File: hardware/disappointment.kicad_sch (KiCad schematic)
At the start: 60 parts, among them J1 Bus_ISA_16bit, J3 Conn_02x10_Odd_Even, J5 ATX-24, U1 F85226AF, U2 L7905

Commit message: pson
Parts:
- added J2: Conn_01x02_Pin, Connector_PinHeader_2.54mm:PinHeader_1x02_P2.54mm_Vertical, symbol Connector:Conn_01x02_Pin
- added R16: 4.7K, Resistor_SMD:R_1206_3216Metric_Pad1.30x1.75mm_HandSolder, symbol Device:R_Small
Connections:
- net +3.3V: now also R16.1
- net GND: now also J2.2 (Pin_2)
- net PWRDN#: now also R16.2
- net at J5.16 (PS_ON#): now also J2.1 (Pin_1)
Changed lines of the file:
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@@
     (stroke (width 0) (type default))
   )
+  (wire (pts (xy 306.07 144.78) (xy 309.88 144.78))
+    (stroke (width 0) (type default))
+  )
   (wire (pts (xy 478.79 162.56) (xy 481.33 162.56))
     (stroke (width 0) (type default))
@@
     (stroke (width 0) (type default))
   )
-  (wire (pts (xy 313.69 264.16) (xy 321.31 264.16))
+  (wire (pts (xy 309.88 264.16) (xy 321.31 264.16))
     (stroke (width 0) (type default))
   )
@@
     )
   )
+  (symbol (lib_name "+3.3V_9") (lib_id "power:+3.3V") (at 309.88 259.08 0) (unit 1)
+    (in_bom yes) (on_board yes) (dnp no) (fields_autoplaced)
+    (property "Reference" "#PWR018" (at 309.88 262.89 0)
+      (effects (font (size 1.27 1.27)) hide)
+    )
+    (property "Value" "+3.3V" (at 309.88 255.27 0)
+      (effects (font (size 1.27 1.27)))
+    )
+    (property "Footprint" "" (at 309.88 259.08 0)
+      (effects (font (size 1.27 1.27)) hide)
+    )
+    (property "Datasheet" "" (at 309.88 259.08 0)
+      (effects (font (size 1.27 1.27)) hide)
+    )
+    (pin "1")
+    (instances
+      (project "disappointment"
+        (path "/a1292a79-9ba8-4ff9-9f33-166186bea326"
+          (reference "#PWR018") (unit 1)
+        )
+      )
+    )
+  )
   (symbol (lib_name "GND_4") (lib_id "power:GND") (at 331.47 209.55 0) (unit 1)
     (in_bom yes) (on_board yes) (dnp no)
@@
     )
   )
+  (symbol (lib_name "GND_3") (lib_id "power:GND") (at 306.07 147.32 0) (unit 1)
+    (in_bom yes) (on_board yes) (dnp no) (fields_autoplaced)
+    (property "Reference" "#PWR019" (at 306.07 153.67 0)
+      (effects (font (size 1.27 1.27)) hide)
+    )
+    (property "Value" "GND" (at 306.07 152.4 0)
+      (effects (font (size 1.27 1.27)) hide)
+    )
+    (property "Footprint" "" (at 306.07 147.32 0)
+      (effects (font (size 1.27 1.27)) hide)
+    )
+    (property "Datasheet" "" (at 306.07 147.32 0)
+      (effects (font (size 1.27 1.27)) hide)
+    )
+    (pin "1")
+    (instances
+      (project "disappointment"
+        (path "/a1292a79-9ba8-4ff9-9f33-166186bea326"
+          (reference "#PWR019") (unit 1)
+        )
+      )
+    )
+  )
   (symbol (lib_id "Device:R_Pack04") (at 476.25 170.18 90) (unit 1)
     (in_bom yes) (on_board yes) (dnp no)
@@
     )
   )
+  (symbol (lib_id "Connector:Conn_01x02_Pin") (at 300.99 144.78 0) (unit 1)
+    (in_bom yes) (on_board yes) (dnp no)
+    (property "Reference" "J2" (at 300.99 135.89 0)
+      (effects (font (size 1.27 1.27)))
+    )
+    (property "Value" "Conn_01x02_Pin" (at 299.72 138.43 0)
+      (effects (font (size 1.27 1.27)))
+    )
+    (property "Footprint" "Connector_PinHeader_2.54mm:PinHeader_1x02_P2.54mm_Vertical" (at 300.99 144.78 0)
+      (effects (font (size 1.27 1.27)) hide)
+    )
+    (property "Datasheet" "~" (at 300.99 144.78 0)
+      (effects (font (size 1.27 1.27)) hide)
+    )
+    (pin "1")
+    (pin "2")
+    (instances
+      (project "disappointment"
+        (path "/a1292a79-9ba8-4ff9-9f33-166186bea326"
+          (reference "J2") (unit 1)
+        )
+      )
+    )
+  )
   (symbol (lib_id "Device:R_Small") (at 407.67 152.4 270) (unit 1)
     (in_bom yes) (on_board yes) (dnp no)
@@
         )
       )
+    )
+  )
+  (symbol (lib_id "Device:R_Small") (at 309.88 261.62 0) (unit 1)
+    (in_bom yes) (on_board yes) (dnp no)
+    (property "Reference" "R16" (at 307.34 266.7 90)
+      (effects (font (size 1.27 1.27)) (justify left))
+    )
+    (property "Value" "4.7K" (at 307.34 261.62 90)
+      (effects (font (size 1.27 1.27)) (justify left))
+    )
+    (property "Footprint" "Resistor_SMD:R_1206_3216Metric_Pad1.30x1.75mm_HandSolder" (at 309.88 261.62 0)
+      (effects (font (size 1.27 1.27)) hide)
+    )
+    (property "Datasheet" "~" (at 309.88 261.62 0)
+      (effects (font (size 1.27 1.27)) hide)
+    )
+    (pin "1")
+    (pin "2")
+    (instances
+      (project "disappointment"
+        (path "/a1292a79-9ba8-4ff9-9f33-166186bea326"
+          (reference "R16") (unit 1)
+        )
+      )

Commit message: what a... letdown?
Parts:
- J2: value Conn_01x02_Pin -> PS_ON
- J3: value Conn_02x10_Odd_Even -> LPC
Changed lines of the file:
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@@
   (junction (at 396.24 167.64) (diameter 0) (color 0 0 0 0)
   )
-  (junction (at 345.44 149.86) (diameter 0) (color 0 0 0 0)
-  )
   (junction (at 481.33 193.04) (diameter 0) (color 0 0 0 0)
   )
   (junction (at 124.46 224.79) (diameter 0) (color 0 0 0 0)
   )
-  (junction (at 345.44 152.4) (diameter 0) (color 0 0 0 0)
-  )
   (junction (at 124.46 186.69) (diameter 0) (color 0 0 0 0)
   )
@@
     (stroke (width 0) (type default))
   )
-  (wire (pts (xy 340.36 152.4) (xy 345.44 152.4))
-    (stroke (width 0) (type default))
-  )
   (wire (pts (xy 416.56 139.7) (xy 425.45 139.7))
     (stroke (width 0) (type default))
@@
     (stroke (width 0) (type default))
   )
-  (wire (pts (xy 339.09 149.86) (xy 345.44 149.86))
-    (stroke (width 0) (type default))
-  )
   (label "IRQ7" (at 425.45 190.5 180) (fields_autoplaced)
     (effects (font (size 1.27 1.27)) (justify right bottom))
@@
       (effects (font (size 1.27 1.27)))
     )
-    (property "Value" "Conn_01x02_Pin" (at 299.72 138.43 0)
+    (property "Value" "PS_ON" (at 299.72 138.43 0)
       (effects (font (size 1.27 1.27)))
     )
@@
   (symbol (lib_id "Connector_Generic:Conn_02x10_Odd_Even") (at 326.39 251.46 0) (unit 1)
     (in_bom yes) (on_board yes) (dnp no) (fields_autoplaced)
-    (property "Reference" "J3" (at 327.66 234.95 0)
+    (property "Reference" "J3" (at 327.66 236.22 0)
       (effects (font (size 1.27 1.27)))
     )
-    (property "Value" "Conn_02x10_Odd_Even" (at 327.66 237.49 0)
+    (property "Value" "LPC" (at 327.66 238.76 0)
       (effects (font (size 1.27 1.27)))
     )

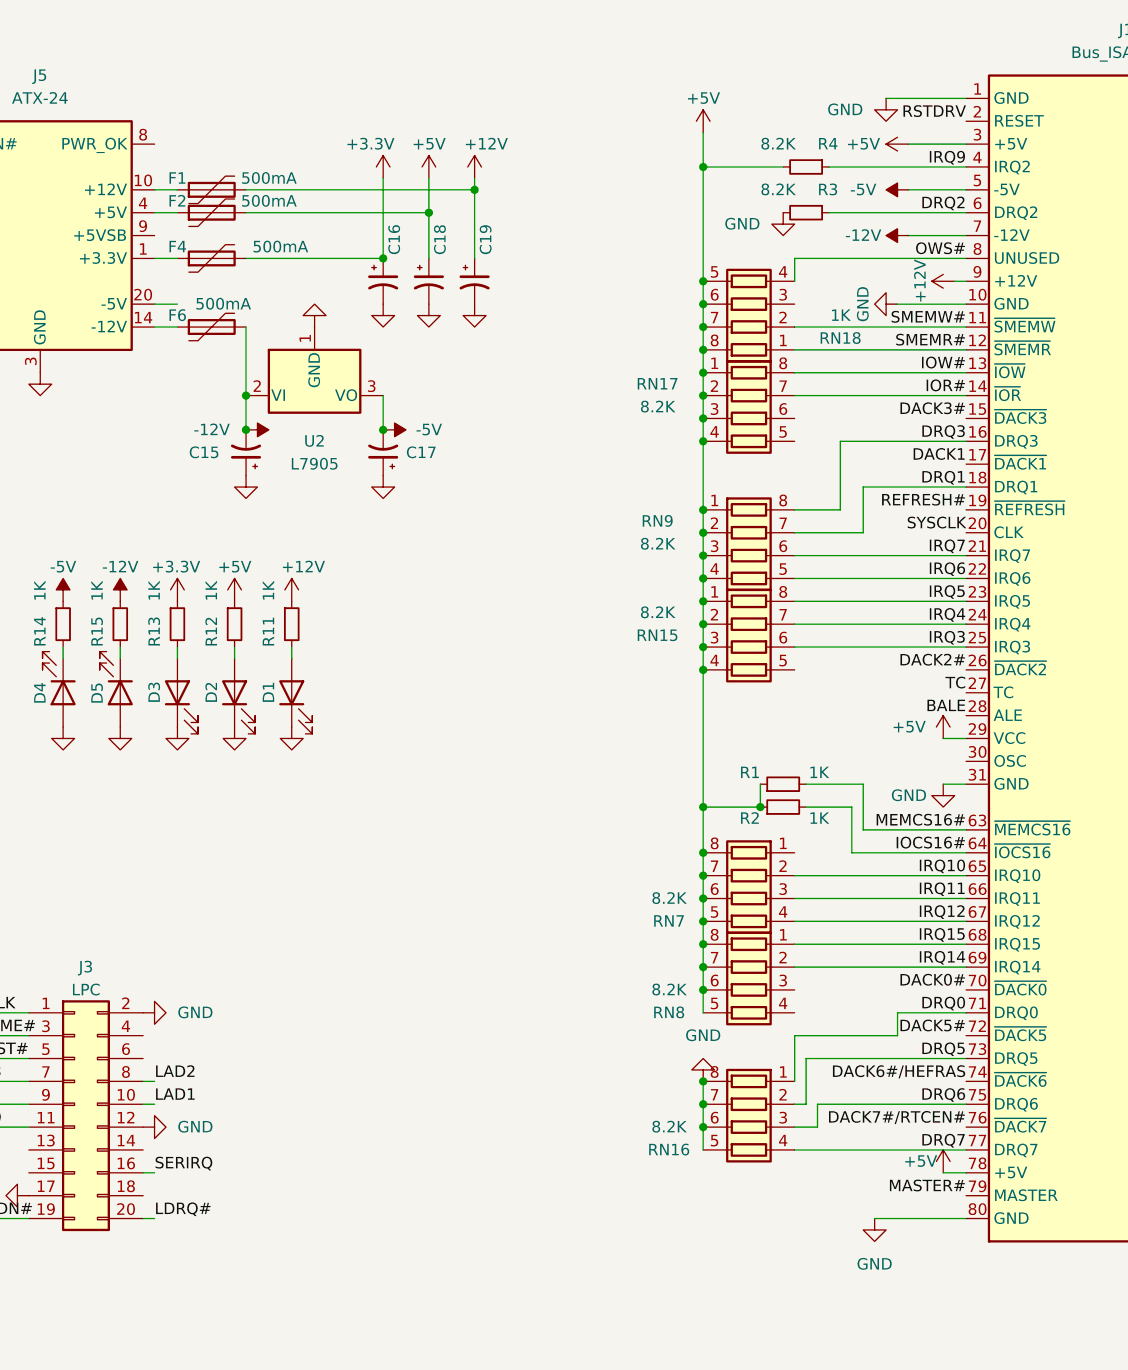
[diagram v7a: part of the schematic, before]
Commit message: added the correct resistors
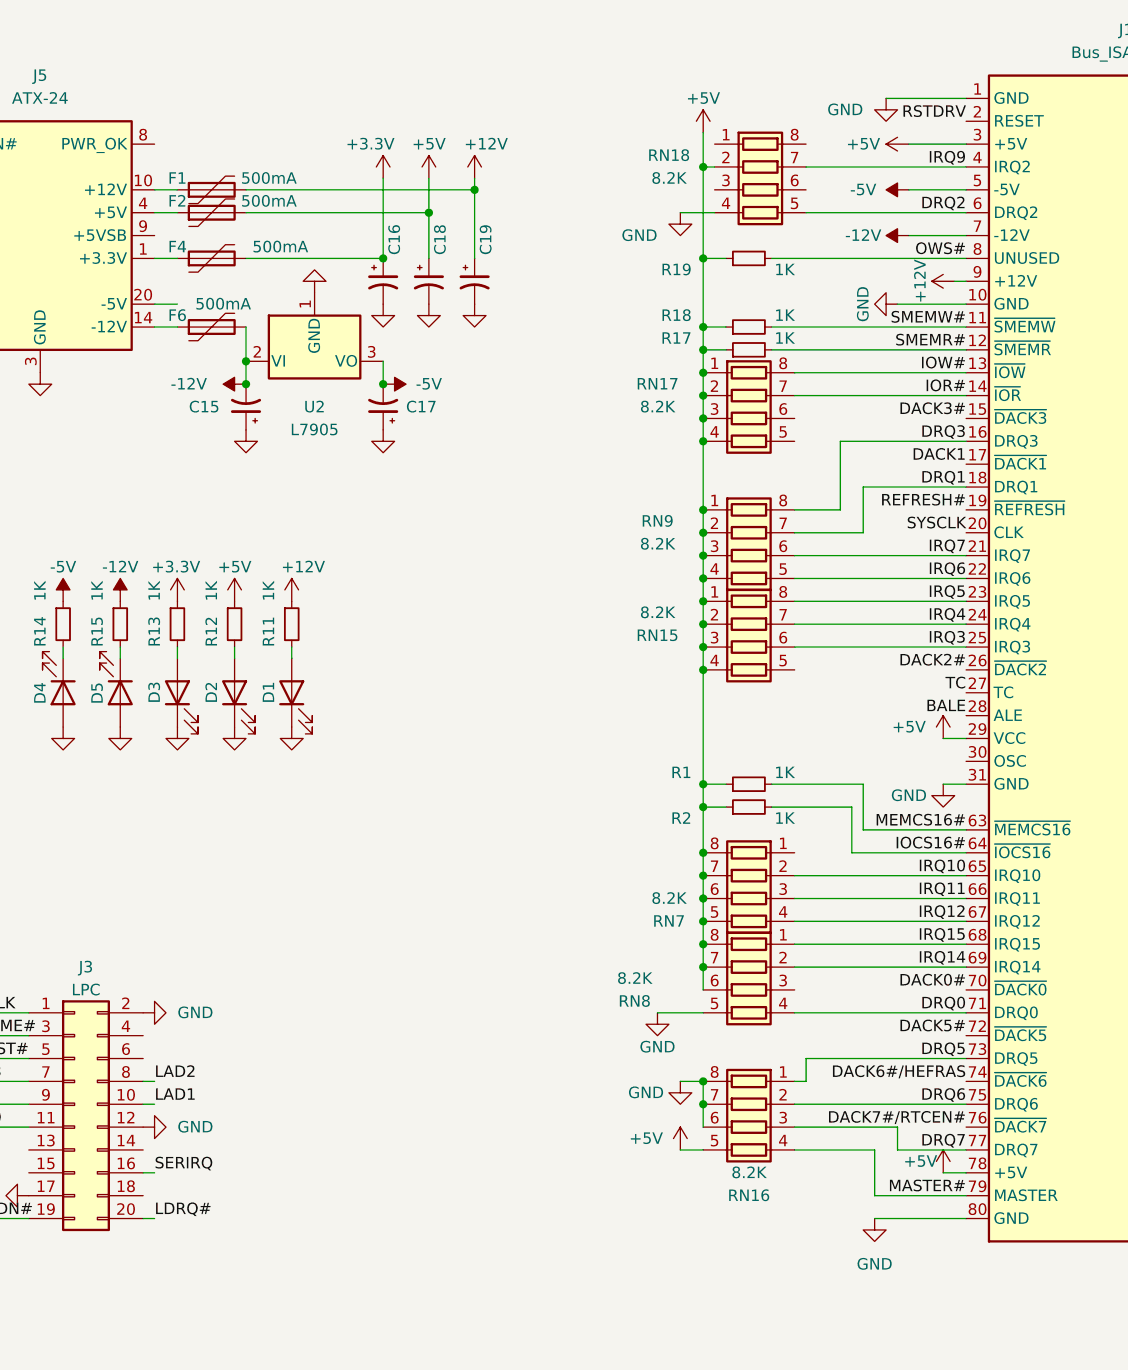
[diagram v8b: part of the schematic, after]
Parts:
- removed R3, R4: 8.2K, Resistor_SMD:R_1206_3216Metric_Pad1.30x1.75mm_HandSolder, symbol Device:R_Small
- added R17, R18, R19: 1K, Resistor_SMD:R_1206_3216Metric_Pad1.30x1.75mm_HandSolder, symbol Device:R_Small
- RN18: value 1K -> 8.2K
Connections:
- net +5V: now also RN16.5 (R4.2), RN18.2 (R2.1), R17.1, R18.1, R19.1; no longer RN18.5 (R4.2), RN18.6 (R3.2), RN18.7 (R2.2), RN18.8 (R1.2), RN8.5 (R4.2)
- net DRQ0: now also RN8.4 (R4.1); no longer RN16.1 (R1.1)
- net DRQ2: now also RN18.5 (R4.2)
- net DRQ5: now also RN16.1 (R1.1); no longer RN16.2 (R2.1)
- net DRQ6: now also RN16.2 (R2.1); no longer RN16.3 (R3.1)
- net DRQ7: now also RN16.3 (R3.1); no longer RN16.4 (R4.1)
- net GND: now also RN18.4 (R4.1), RN8.5 (R4.2); no longer RN16.5 (R4.2)
- net IRQ9: now also RN18.7 (R2.2)
- net MASTER#: now also RN16.4 (R4.1)
- net OWS#: now also R19.2; no longer RN18.4 (R4.1)
- net SMEMR#: now also R17.2; no longer RN18.1 (R1.1)
- net SMEMW#: now also R18.2; no longer RN18.2 (R2.1)
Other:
- moved on the sheet: C15, C17, R1, R2, U2
